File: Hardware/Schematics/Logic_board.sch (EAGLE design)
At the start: 40 parts, among them IC1 ADUM1250, J1 1X2-3.5MM, U1 ESP-32S

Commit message: Relay board placement mostly done. Routing ~50% done.
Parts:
- added C9: 100nF, rcl:C-EUC0805
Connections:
- net GND: now also C9.2
- net VCC: now also C9.1

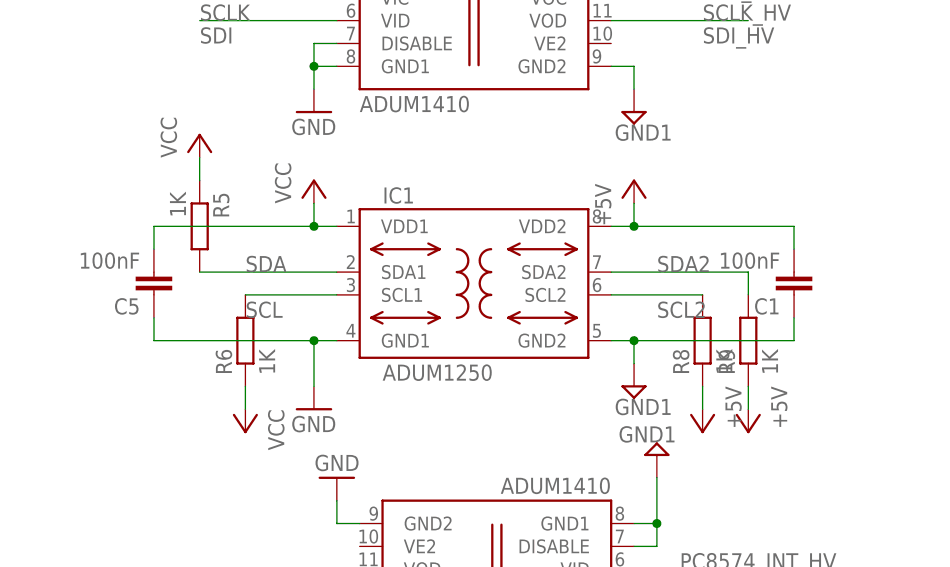
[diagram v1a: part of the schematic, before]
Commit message: Power board routing done. Still missing adjustments of soldermask and silkscreen on both powerboard and logic board.
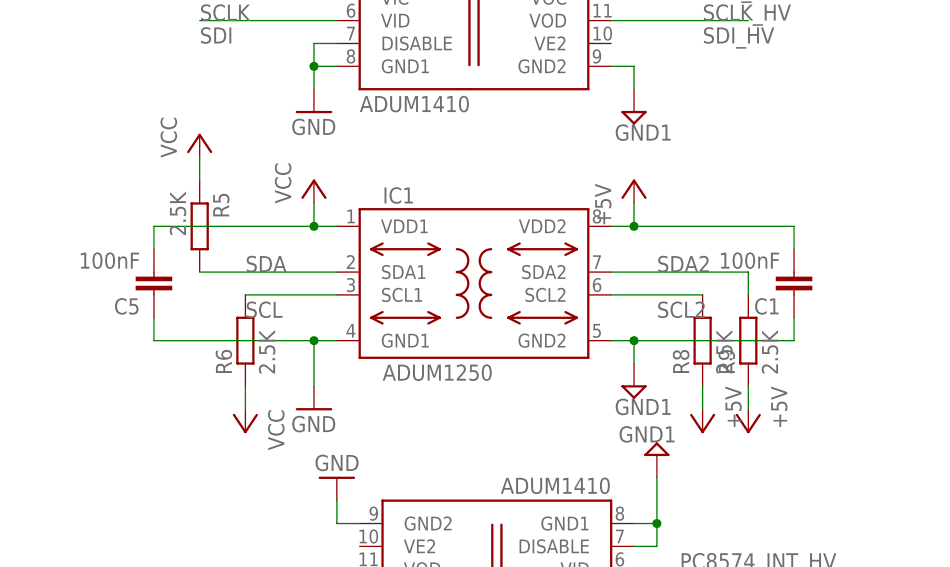
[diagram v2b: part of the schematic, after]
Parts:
- R5, R6, R8, R9: value 1K -> 2.5K
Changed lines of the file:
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@@
 <part name="P+7" library="supply1" deviceset="VCC" device=""/>
 <part name="JP1" library="pinhead" library_urn="urn:adsk.eagle:library:325" deviceset="PINHD-2X9" device="/90"/>
-<part name="R8" library="rcl" deviceset="R-EU_" device="R0805" value="1K"/>
-<part name="R9" library="rcl" deviceset="R-EU_" device="R0805" value="1K"/>
+<part name="R8" library="rcl" deviceset="R-EU_" device="R0805" value="2.5K"/>
+<part name="R9" library="rcl" deviceset="R-EU_" device="R0805" value="2.5K"/>
 <part name="P+22" library="supply1" library_urn="urn:adsk.eagle:library:371" deviceset="+5V" device=""/>
 <part name="P+23" library="supply1" library_urn="urn:adsk.eagle:library:371" deviceset="+5V" device=""/>
-<part name="R5" library="rcl" deviceset="R-EU_" device="R0805" value="1K"/>
-<part name="R6" library="rcl" deviceset="R-EU_" device="R0805" value="1K"/>
+<part name="R5" library="rcl" deviceset="R-EU_" device="R0805" value="2.5K"/>
+<part name="R6" library="rcl" deviceset="R-EU_" device="R0805" value="2.5K"/>
 <part name="P+12" library="supply1" deviceset="VCC" device=""/>
 <part name="P+15" library="supply1" deviceset="VCC" device=""/>

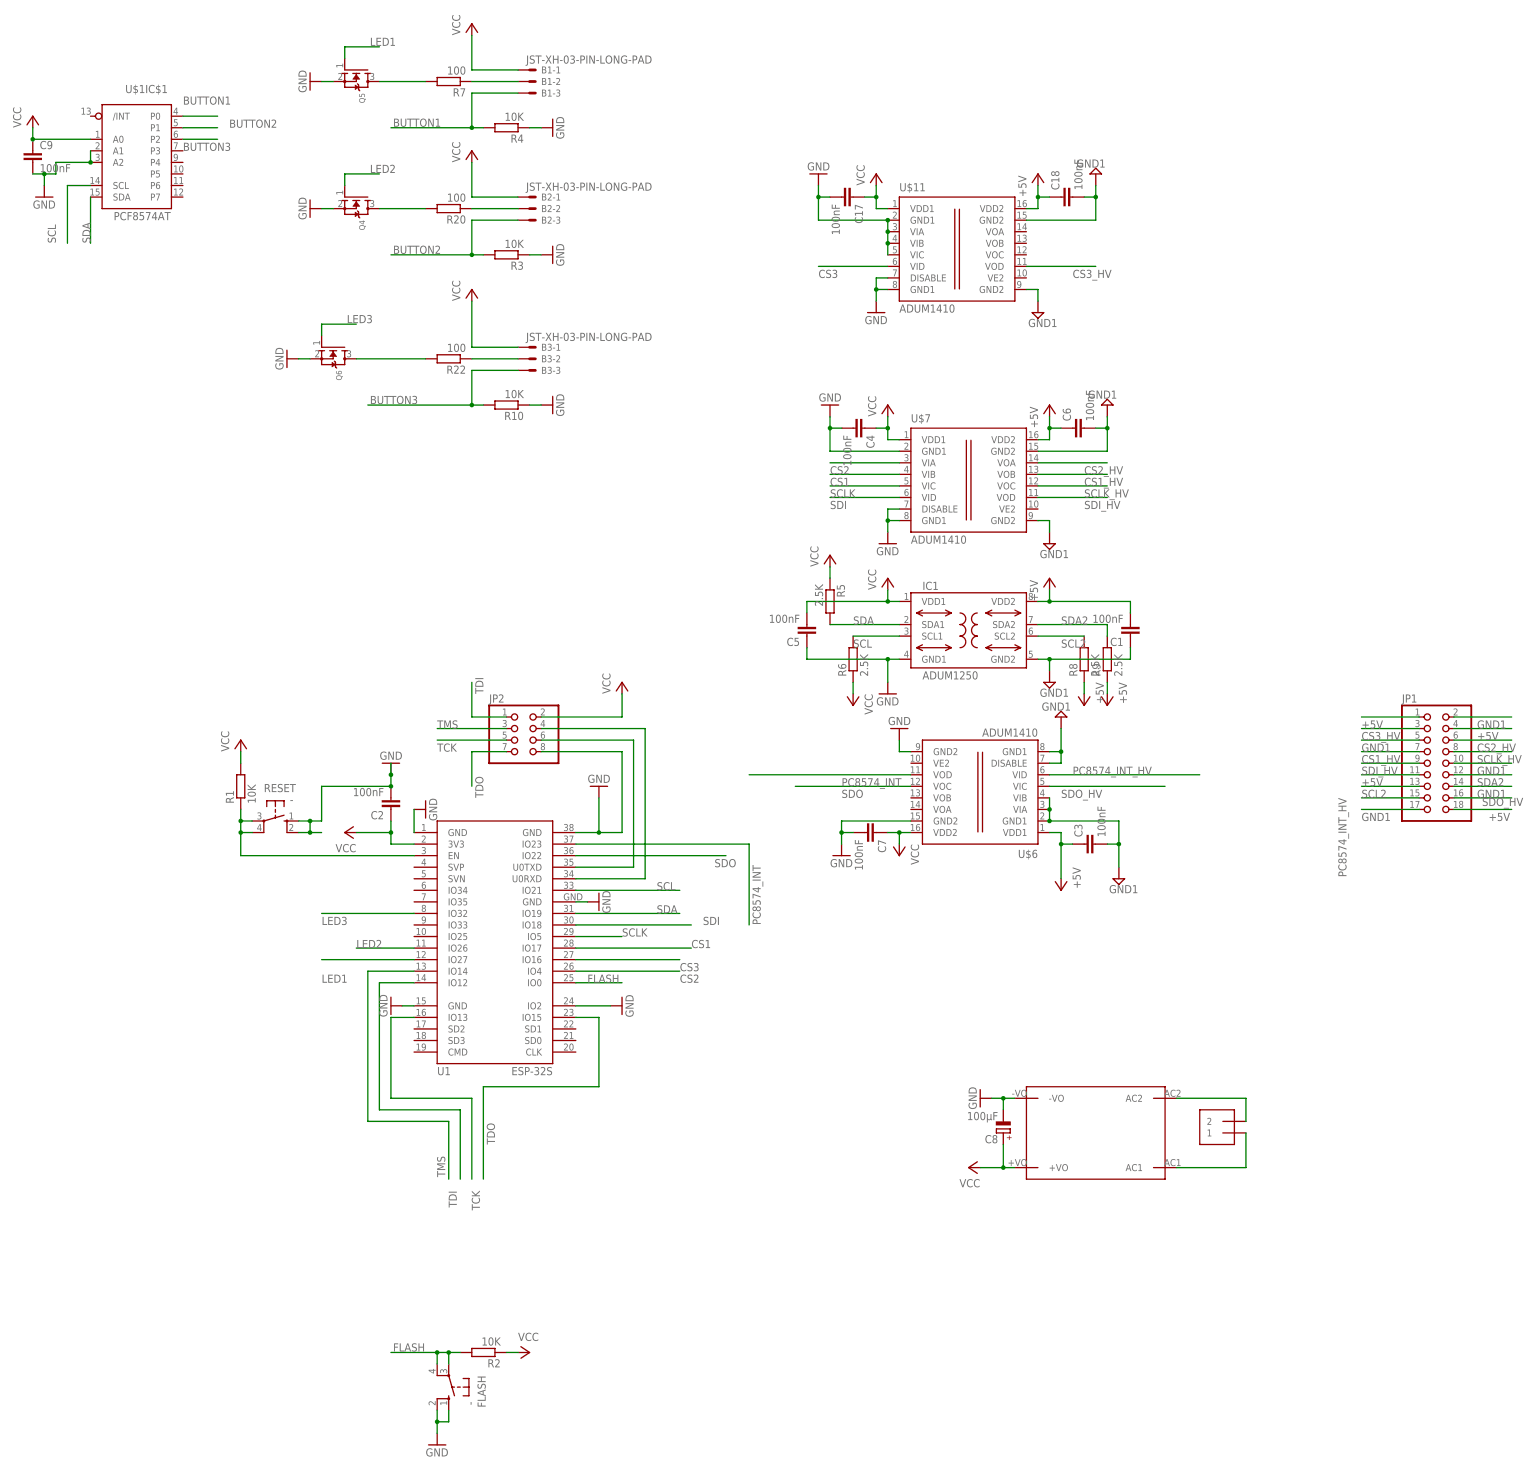
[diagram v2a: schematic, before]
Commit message: Made Logic Board a bit smaller.
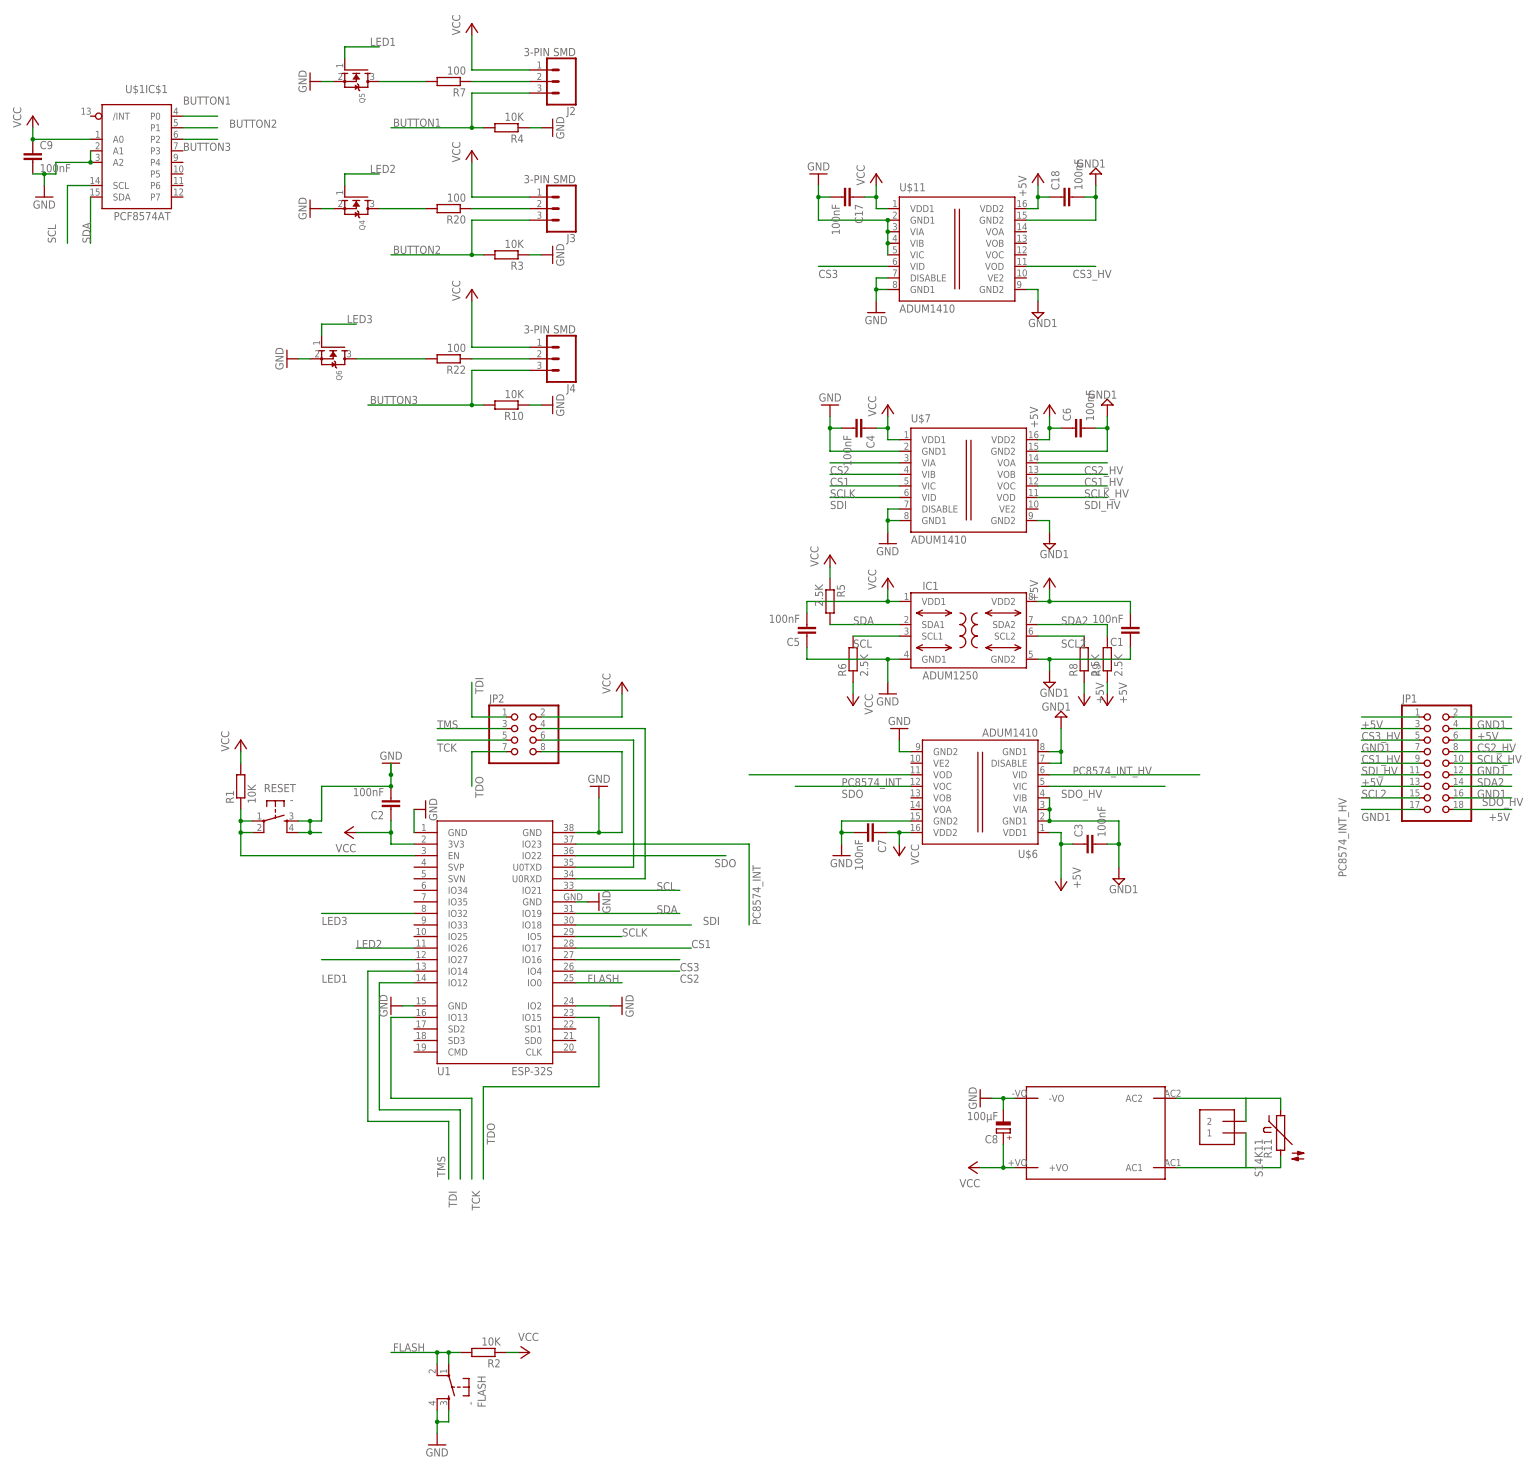
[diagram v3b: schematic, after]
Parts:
- removed B1, B2, B3: JST-XH-03-PIN-LONG-PAD, Rembrandt:JST-XH-03-PIN-LONG-PAD
- added J2, J3, J4: 3-PIN SMD, SparkFun-Connectors:CONN_03JST-SMD
- added R11: S14K11, varistor:S14K11
- C8: device rcl:CPOL-EUE3.5-8 -> rcl:CPOL-EUE2.5-6
- FLASH, RESET: device switch-omron:10-XX -> switch-tact:DTSM-6
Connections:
- net AC1: now also R11.2
- net AC2: now also R11.1
- net BUTTON1: now also J2.3; no longer B1-3.S
- net BUTTON2: now also J3.3; no longer B2-3.S
- net BUTTON3: now also J4.3; no longer B3-3.S
- net FLASH: now also FLASH.1, FLASH.2; no longer FLASH.P, FLASH.P1
- net GND: now also FLASH.3, FLASH.4, RESET.3, RESET.4; no longer FLASH.S, FLASH.S1, RESET.S, RESET.S1
- net N$11: now also J4.2; no longer B3-2.S
- net N$66: now also RESET.1, RESET.2; no longer RESET.P, RESET.P1
- net N$7: now also J3.2; no longer B2-2.S
- net N$9: now also J2.2; no longer B1-2.S
- net VCC: now also J2.1, J3.1, J4.1; no longer B1-1.S, B2-1.S, B3-1.S
